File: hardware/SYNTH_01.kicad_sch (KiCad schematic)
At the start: 56 parts, among them J1 RPI4_GPIO_40, SW1 SW_Push_45deg, SW10 SW_Push_45deg, SW11 SW_Push_45deg, SW12 SW_Push_45deg, SW13 SW_Push_45deg, SW14 SW_Push_45deg, SW15 SW_Push_45deg, SW16 SW_Push_45deg, SW17 SW_Push_45deg, SW18 SW_Push_45deg, SW19 SW_Push_45deg, SW2 SW_Push_45deg, SW20 SW_Push_45deg, SW21 SW_Push_45deg, SW3 SW_Push_45deg, SW4 SW_Push_45deg, SW5 SW_Push_45deg, SW6 SW_Push_45deg, SW7 SW_Push_45deg, SW8 SW_Push_45deg, SW9 SW_Push_45deg, U1 MCP23017-E/SP, U2 MCP23017-E/SP

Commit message: [PCB] adding PWR_FLAG to Pi4 +3v3 and GND to indicate KiCAD these are the power sources for the board
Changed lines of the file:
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@@
 	)
 	(junction
+		(at 179.07 35.56)
+		(diameter 0)
+		(color 0 0 0 0)
+	)
+	(junction
+		(at 162.56 30.48)
+		(diameter 0)
+		(color 0 0 0 0)
+	)
+	(junction
 		(at 59.69 195.58)
 		(diameter 0)
@@
 	(wire
 		(pts
+			(xy 162.56 27.94) (xy 162.56 30.48)
+		)
+		(stroke
+			(width 0)
+			(type default)
+		)
+	)
+	(wire
+		(pts
 			(xy 267.97 129.54) (xy 271.78 129.54)
 		)
@@
 	(wire
 		(pts
+			(xy 181.61 33.02) (xy 179.07 33.02)
+		)
+		(stroke
+			(width 0)
+			(type default)
+		)
+	)
+	(wire
+		(pts
 			(xy 135.89 93.98) (xy 156.21 93.98)
 		)
@@
 	(wire
 		(pts
+			(xy 179.07 33.02) (xy 179.07 35.56)
+		)
+		(stroke
+			(width 0)
+			(type default)
+		)
+	)
+	(wire
+		(pts
 			(xy 54.61 68.58) (xy 54.61 81.28)
 		)
@@
 	(wire
 		(pts
+			(xy 158.75 27.94) (xy 162.56 27.94)
+		)
+		(stroke
+			(width 0)
+			(type default)
+		)
+	)
+	(wire
+		(pts
 			(xy 110.49 119.38) (xy 135.89 119.38)
 		)
@@
 	)
 	(symbol
+		(lib_id "power:PWR_FLAG")
+		(at 181.61 33.02 0)
+		(unit 1)
+		(body_style 1)
+		(exclude_from_sim no)
+		(in_bom yes)
+		(on_board yes)
+		(in_pos_files yes)
+		(dnp no)
+		(fields_autoplaced yes)
+		(property "Reference" "#FLG02"
+			(at 181.61 31.115 0)
+			(hide yes)
+			(show_name no)
+			(do_not_autoplace no)
+			(effects
+				(font
+					(size 1.27 1.27)
+				)
+			)
+		)
+		(property "Value" "PWR_FLAG"
+			(at 181.61 27.94 0)
+			(show_name no)
+			(do_not_autoplace no)
+			(effects
+				(font
+					(size 1.27 1.27)
+				)
+			)
+		)
+		(property "Footprint" ""
+			(at 181.61 33.02 0)
+			(hide yes)
+			(show_name no)
+			(do_not_autoplace no)
+			(effects
+				(font
+					(size 1.27 1.27)
+				)
+			)
+		)
+		(property "Datasheet" ""
+			(at 181.61 33.02 0)
+			(hide yes)
+			(show_name no)
+			(do_not_autoplace no)
+			(effects
+				(font
+					(size 1.27 1.27)
+				)
+			)
+		)
+		(property "Description" "Special symbol for telling ERC where power comes from"
+			(at 181.61 33.02 0)
+			(hide yes)
+			(show_name no)
+			(do_not_autoplace no)
+			(effects
+				(font
+					(size 1.27 1.27)
+				)
+			)
+		)
+		(pin "1"
+		)
+		(instances
+			(project "SYNTH_01"
+				(path "/8736209f-7c7b-4c76-92ee-96040748110a"
+					(reference "#FLG02")
+					(unit 1)
+				)
+			)
+		)
+	)
+	(symbol
 		(lib_id "Device:RotaryEncoder_Switch")
 		(at 38.1 152.4 0)
@@
 					(unit 1)
 				)
+			)
+		)
+	)
+	(symbol
+		(lib_id "power:PWR_FLAG")
+		(at 158.75 27.94 0)
+		(unit 1)
+		(body_style 1)
+		(exclude_from_sim no)
+		(in_bom yes)
+		(on_board yes)
+		(in_pos_files yes)
+		(dnp no)
+		(fields_autoplaced yes)
+		(property "Reference" "#FLG01"
+			(at 158.75 26.035 0)
+			(hide yes)
+			(show_name no)
+			(do_not_autoplace no)
+			(effects
+				(font
+					(size 1.27 1.27)
+				)
+			)
+		)
+		(property "Value" "PWR_FLAG"
+			(at 158.75 22.86 0)
+			(show_name no)
+			(do_not_autoplace no)
+			(effects
+				(font
+					(size 1.27 1.27)
+				)
+			)
+		)
+		(property "Footprint" ""
+			(at 158.75 27.94 0)
+			(hide yes)
+			(show_name no)
+			(do_not_autoplace no)
+			(effects
+				(font
+					(size 1.27 1.27)
+				)
+			)
+		)
+		(property "Datasheet" ""
+			(at 158.75 27.94 0)
+			(hide yes)
+			(show_name no)
+			(do_not_autoplace no)
+			(effects
+				(font
+					(size 1.27 1.27)
+				)
+			)
+		)
+		(property "Description" "Special symbol for telling ERC where power comes from"
+			(at 158.75 27.94 0)
+			(hide yes)
+			(show_name no)
+			(do_not_autoplace no)
+			(effects
+				(font
+					(size 1.27 1.27)
+				)
+			)
+		)
+		(pin "1"
+		)
+		(instances
+			(project "SYNTH_01"
+				(path "/8736209f-7c7b-4c76-92ee-96040748110a"
+					(reference "#FLG01")
+					(unit 1)
+				)

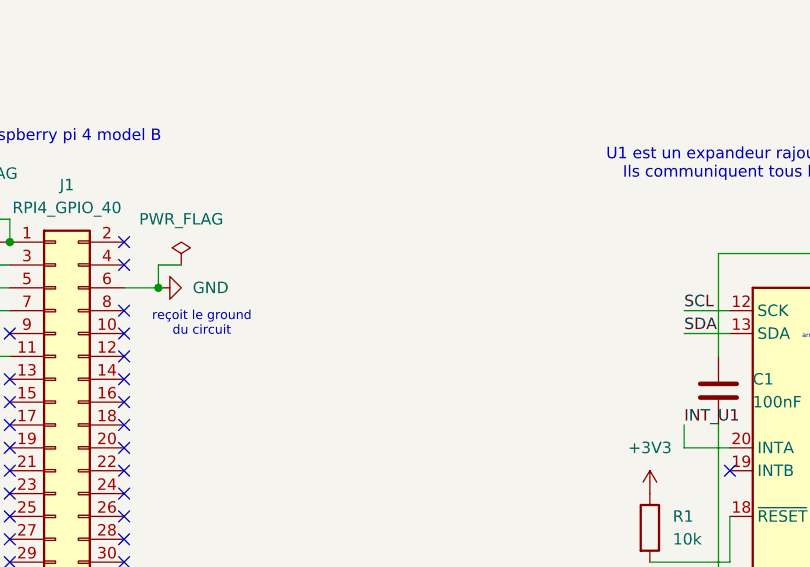
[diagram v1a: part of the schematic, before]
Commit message: [PCB] adding 4 pin connexion representing the OLED
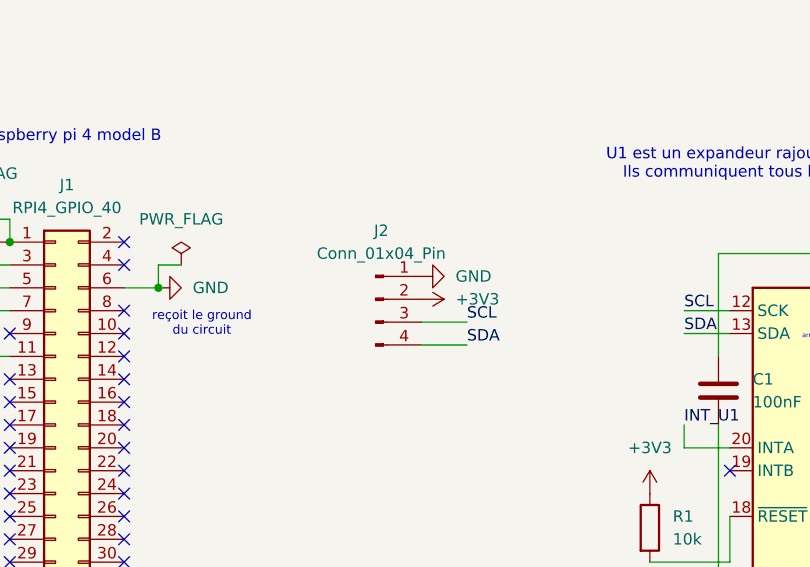
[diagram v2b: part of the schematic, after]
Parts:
- added J2: Conn_01x04_Pin, symbol Connector:Conn_01x04_Pin
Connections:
- net +3V3: now also J2.2 (Pin_2)
- net GND: now also J2.1 (Pin_1)
- net SCL: now also J2.3 (Pin_3)
- net SDA: now also J2.4 (Pin_4)

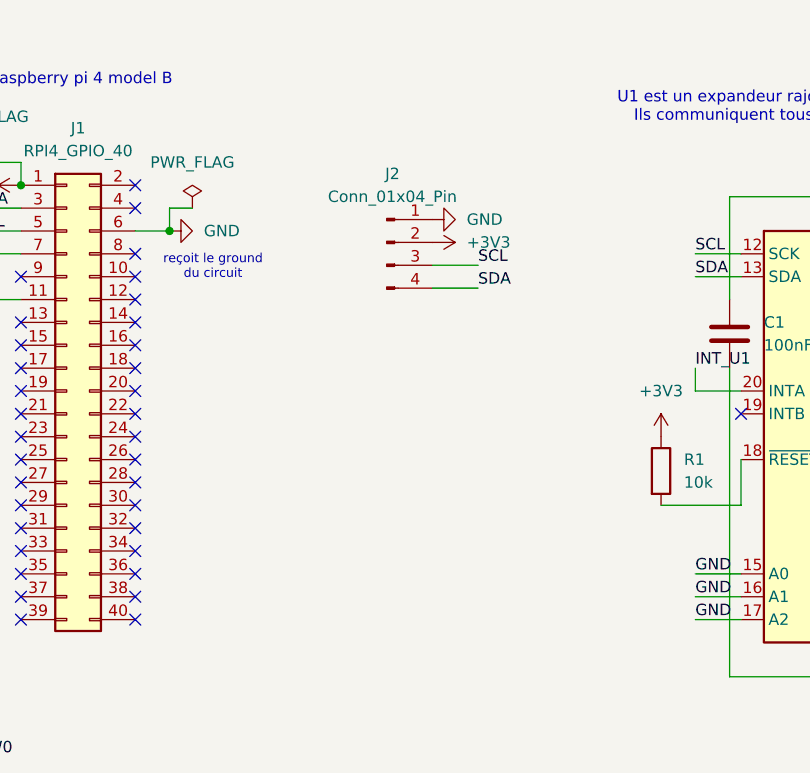
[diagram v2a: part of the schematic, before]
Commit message: [PCB] updating PCB schematic with choosen OLED model being SSD1306 12832 0.91 IIC i2C
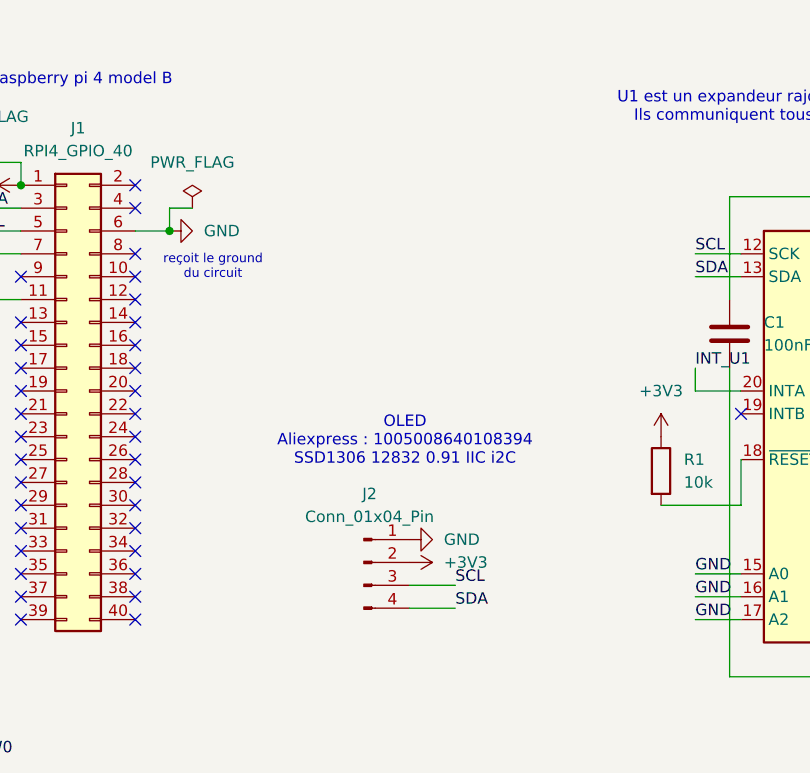
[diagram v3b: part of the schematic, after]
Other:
- note added: "OLED Aliexpress : 1005008640108394 SSD1306 12832 0.91 IIC i2C"
- moved on the sheet: J2
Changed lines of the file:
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@@
 		)
 	)
+	(text "OLED\nAliexpress : 1005008640108394\nSSD1306 12832 0.91 IIC i2C"
+		(exclude_from_sim no)
+		(at 205.232 58.928 0)
+		(effects
+			(font
+				(size 1.27 1.27)
+			)
+		)
+	)
 	(junction
 		(at 80.01 157.48)
@@
 	(wire
 		(pts
-			(xy 208.28 41.91) (xy 213.36 41.91)
+			(xy 205.74 77.47) (xy 210.82 77.47)
 		)
 		(stroke
@@
 	(wire
 		(pts
-			(xy 213.36 39.37) (xy 208.28 39.37)
+			(xy 210.82 74.93) (xy 205.74 74.93)
 		)
 		(stroke
@@
 	)
 	(label "SCL"
-		(at 213.36 39.37 0)
+		(at 210.82 74.93 0)
 		(effects
 			(font
@@
 	)
 	(label "SDA"
-		(at 213.36 41.91 0)
+		(at 210.82 77.47 0)
 		(effects
 			(font
@@
 	(symbol
 		(lib_id "Connector:Conn_01x04_Pin")
-		(at 203.2 36.83 0)
+		(at 200.66 72.39 0)
 		(unit 1)
 		(body_style 1)
@@
 		(fields_autoplaced yes)
 		(property "Reference" "J2"
-			(at 203.835 29.21 0)
+			(at 201.295 64.77 0)
 			(show_name no)
 			(do_not_autoplace no)
@@
 		)
 		(property "Value" "Conn_01x04_Pin"
-			(at 203.835 31.75 0)
+			(at 201.295 67.31 0)
 			(show_name no)
 			(do_not_autoplace no)
@@
 		)
 		(property "Footprint" ""
-			(at 203.2 36.83 0)
+			(at 200.66 72.39 0)
 			(hide yes)
 			(show_name no)
@@
 		)
 		(property "Datasheet" ""
-			(at 203.2 36.83 0)
+			(at 200.66 72.39 0)
 			(hide yes)
 			(show_name no)
@@
 		)
 		(property "Description" "Generic connector, single row, 01x04, script generated"
-			(at 203.2 36.83 0)
+			(at 200.66 72.39 0)
 			(hide yes)
 			(show_name no)
@@
 	(symbol
 		(lib_id "power:GND")
-		(at 208.28 34.29 90)
+		(at 205.74 69.85 90)
 		(unit 1)
 		(body_style 1)
@@
 		(fields_autoplaced yes)
 		(property "Reference" "#PWR023"
-			(at 214.63 34.29 0)
+			(at 212.09 69.85 0)
 			(hide yes)
 			(show_name no)
@@
 		)
 		(property "Value" "GND"
-			(at 212.09 34.2899 90)
+			(at 209.55 69.8499 90)
 			(show_name no)
 			(do_not_autoplace no)
@@
 		)
 		(property "Footprint" ""
-			(at 208.28 34.29 0)
+			(at 205.74 69.85 0)
 			(hide yes)
 			(show_name no)
@@
 		)
 		(property "Datasheet" ""
-			(at 208.28 34.29 0)
+			(at 205.74 69.85 0)
 			(hide yes)
 			(show_name no)
@@
 		)
 		(property "Description" "Power symbol creates a global label with name \"GND\" , ground"
-			(at 208.28 34.29 0)
+			(at 205.74 69.85 0)
 			(hide yes)
 			(show_name no)
@@
 	(symbol
 		(lib_id "power:+3V3")
-		(at 208.28 36.83 270)
+		(at 205.74 72.39 270)
 		(unit 1)
 		(body_style 1)
@@
 		(fields_autoplaced yes)
 		(property "Reference" "#PWR024"
-			(at 204.47 36.83 0)
+			(at 201.93 72.39 0)
 			(hide yes)
 			(show_name no)
@@
 		)
 		(property "Value" "+3V3"
-			(at 212.09 36.8299 90)
+			(at 209.55 72.3899 90)
 			(show_name no)
 			(do_not_autoplace no)
@@
 		)
 		(property "Footprint" ""
-			(at 208.28 36.83 0)
+			(at 205.74 72.39 0)
 			(hide yes)
 			(show_name no)
@@
 		)
 		(property "Datasheet" ""
-			(at 208.28 36.83 0)
+			(at 205.74 72.39 0)
 			(hide yes)
 			(show_name no)
@@
 		)
 		(property "Description" "Power symbol creates a global label with name \"+3V3\""
-			(at 208.28 36.83 0)
+			(at 205.74 72.39 0)
 			(hide yes)
 			(show_name no)

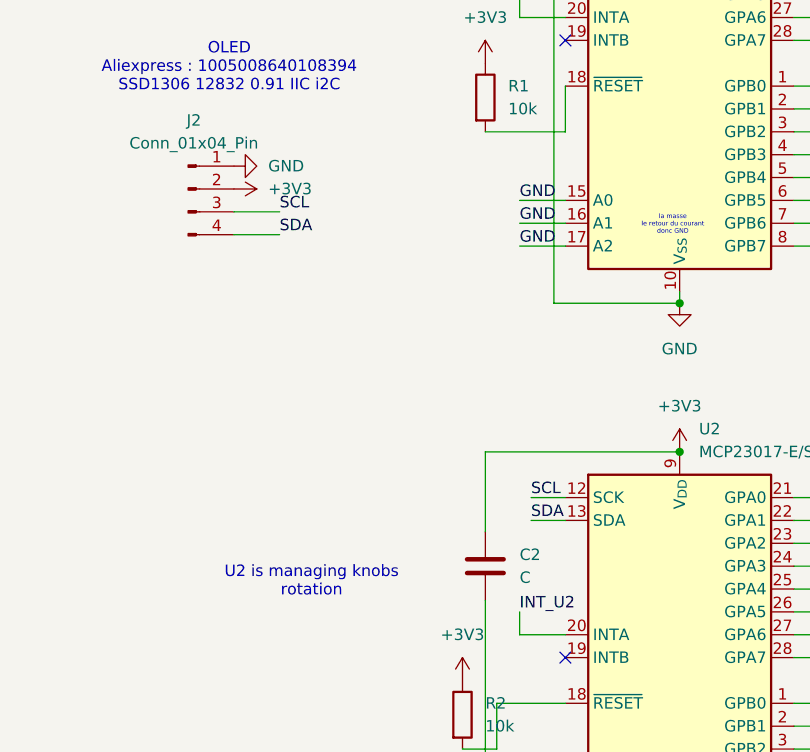
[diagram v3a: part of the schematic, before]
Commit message: [PCB] updating value of condensers to 100nf
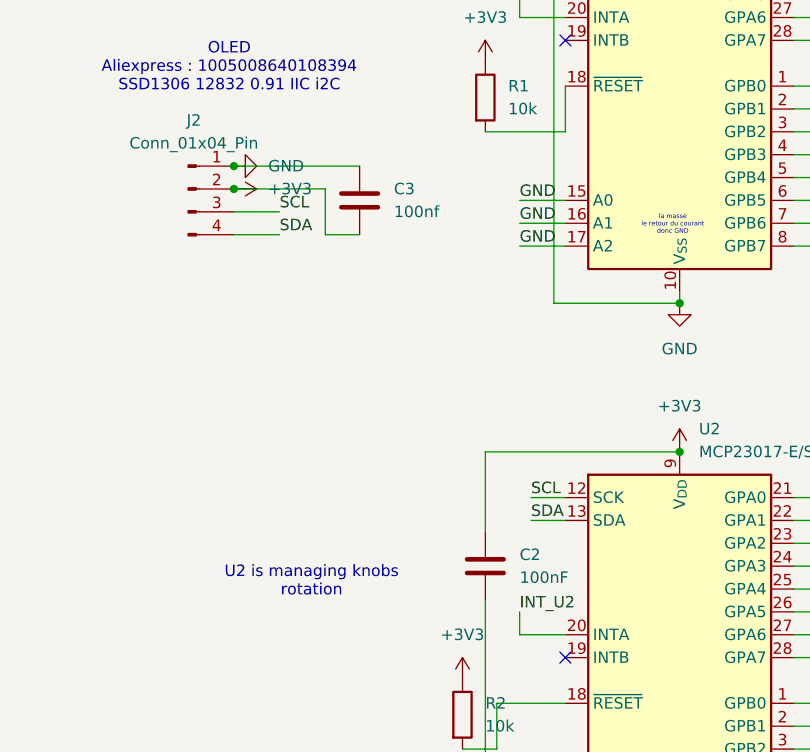
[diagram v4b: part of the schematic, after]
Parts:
- added C3: 100nf, symbol Device:C
- C2: value C -> 100nF
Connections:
- net +3V3: now also C3.2
- net GND: now also C3.1
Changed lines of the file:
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@@
 	)
 	(junction
+		(at 205.74 69.85)
+		(diameter 0)
+		(color 0 0 0 0)
+	)
+	(junction
 		(at 85.09 93.98)
 		(diameter 0)
@@
 	)
 	(junction
+		(at 205.74 72.39)
+		(diameter 0)
+		(color 0 0 0 0)
+	)
+	(junction
 		(at 80.01 81.28)
 		(diameter 0)
@@
 	(wire
 		(pts
+			(xy 215.9 72.39) (xy 205.74 72.39)
+		)
+		(stroke
+			(width 0)
+			(type default)
+		)
+	)
+	(wire
+		(pts
 			(xy 267.97 45.72) (xy 271.78 45.72)
 		)
@@
 	(wire
 		(pts
+			(xy 219.71 77.47) (xy 215.9 77.47)
+		)
+		(stroke
+			(width 0)
+			(type default)
+		)
+	)
+	(wire
+		(pts
 			(xy 237.49 40.64) (xy 242.57 40.64)
 		)
@@
 	(wire
 		(pts
+			(xy 205.74 69.85) (xy 219.71 69.85)
+		)
+		(stroke
+			(width 0)
+			(type default)
+		)
+	)
+	(wire
+		(pts
 			(xy 46.99 88.9) (xy 46.99 90.17)
 		)
@@
 	(wire
 		(pts
+			(xy 215.9 77.47) (xy 215.9 72.39)
+		)
+		(stroke
+			(width 0)
+			(type default)
+		)
+	)
+	(wire
+		(pts
 			(xy 237.49 119.38) (xy 237.49 121.92)
 		)
@@
 	)
 	(symbol
+		(lib_id "Device:C")
+		(at 219.71 73.66 0)
+		(unit 1)
+		(body_style 1)
+		(exclude_from_sim no)
+		(in_bom yes)
+		(on_board yes)
+		(in_pos_files yes)
+		(dnp no)
+		(fields_autoplaced yes)
+		(property "Reference" "C3"
+			(at 223.52 72.3899 0)
+			(show_name no)
+			(do_not_autoplace no)
+			(effects
+				(font
+					(size 1.27 1.27)
+				)
+				(justify left)
+			)
+		)
+		(property "Value" "100nf"
+			(at 223.52 74.9299 0)
+			(show_name no)
+			(do_not_autoplace no)
+			(effects
+				(font
+					(size 1.27 1.27)
+				)
+				(justify left)
+			)
+		)
+		(property "Footprint" ""
+			(at 220.6752 77.47 0)
+			(hide yes)
+			(show_name no)
+			(do_not_autoplace no)
+			(effects
+				(font
+					(size 1.27 1.27)
+				)
+			)
+		)
+		(property "Datasheet" ""
+			(at 219.71 73.66 0)
+			(hide yes)
+			(show_name no)
+			(do_not_autoplace no)
+			(effects
+				(font
+					(size 1.27 1.27)
+				)
+			)
+		)
+		(property "Description" "Unpolarized capacitor"
+			(at 219.71 73.66 0)
+			(hide yes)
+			(show_name no)
+			(do_not_autoplace no)
+			(effects
+				(font
+					(size 1.27 1.27)
+				)
+			)
+		)
+		(pin "2"
+		)
+		(pin "1"
+		)
+		(instances
+			(project "SYNTH_01"
+				(path "/8736209f-7c7b-4c76-92ee-96040748110a"
+					(reference "C3")
+					(unit 1)
+				)
+			)
+		)
+	)
+	(symbol
 		(lib_id "Switch:SW_Push_45deg")
 		(at 57.15 109.22 0)
@@
 			)
 		)
-		(property "Value" "C"
+		(property "Value" "100nF"
 			(at 237.49 115.5699 0)
 			(show_name no)
